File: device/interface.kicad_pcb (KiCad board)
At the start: 2 copper layers, 43.2 x 64.1 mm, 30 parts, among them IC1 ATTINY2313-S, J1 Screw_Terminal_1x02, J2 Screw_Terminal_01x02, P1 CONN_01X06, P2 CONN_02X03, P3 CONN_01X04, U1 L7805, U2 MAX483E, Y1 16MHz

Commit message: pcb update
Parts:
- moved J1 0.63 mm to (99.1, 61.6)
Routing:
- net +5V: track 127.5 -> 128.4 mm
- net /MOSI: track 28.8 -> 29.6 mm
- net /SCK: track 24.3 -> 25.0 mm
- net GND: track 157.1 -> 156.4 mm
- net +24V: track 43.4 -> 44.0 mm
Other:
- outline, holes or cut-outs redrawn
- net class RS-485 added: clearance 0.5, trace_width 0.5, via_dia 0.8, via_drill 0.4

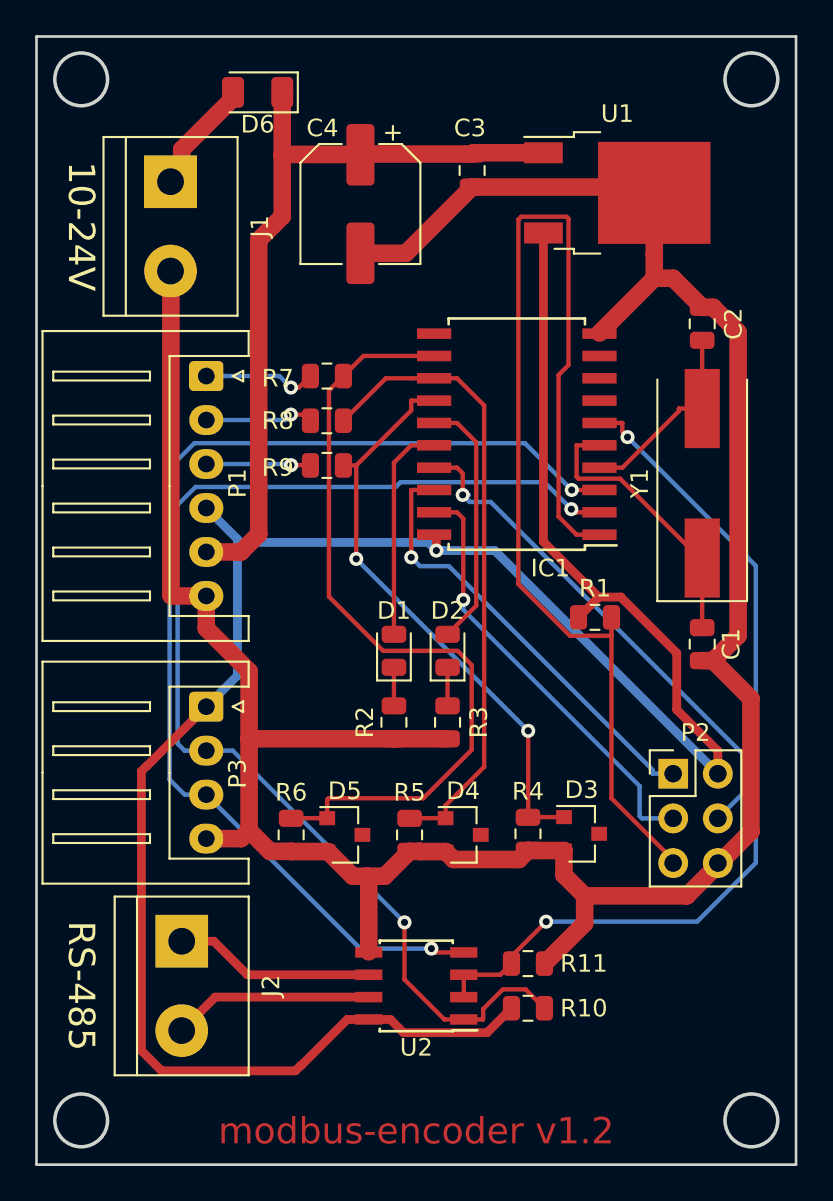
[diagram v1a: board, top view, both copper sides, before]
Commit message: added address switch
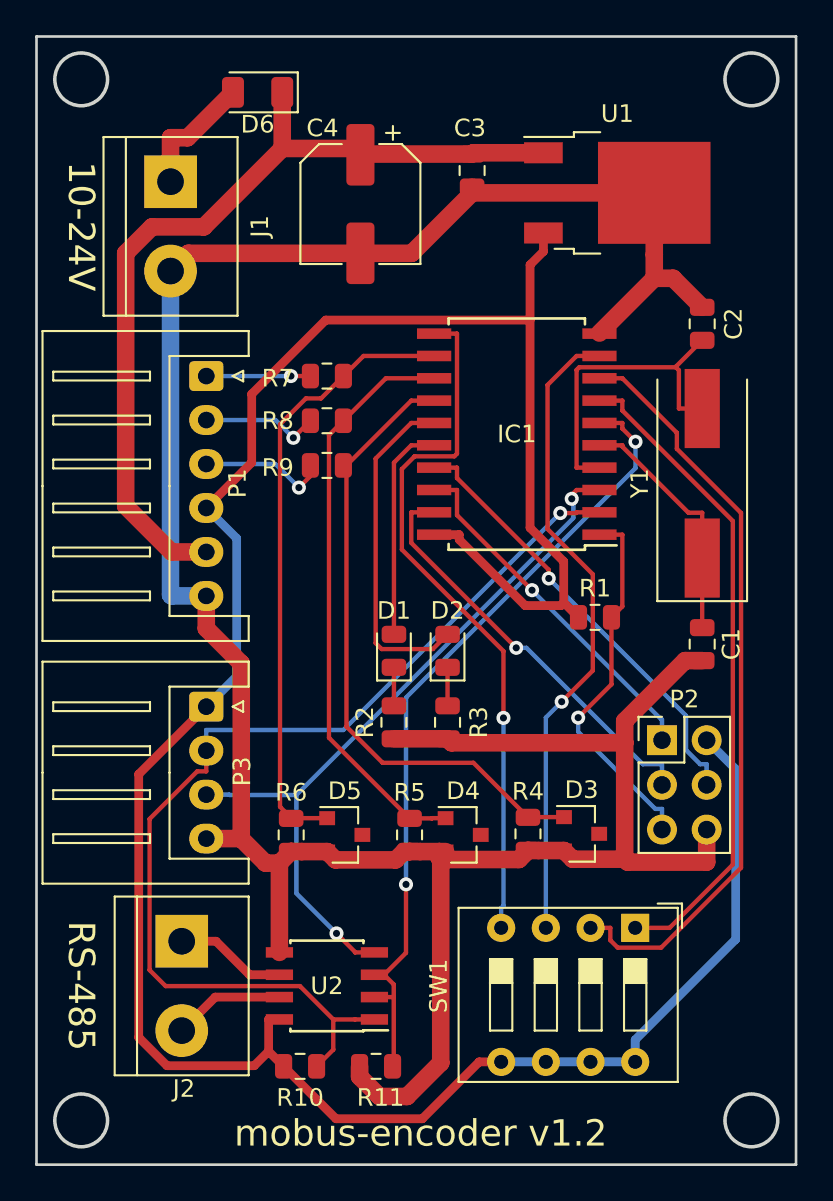
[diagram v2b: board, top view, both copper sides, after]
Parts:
- added SW1: SW_DIP_x04, Button_Switch_THT:SW_DIP_SPSTx04_Slide_9.78x12.34mm_W7.62mm_P2.54mm, F.Cu at (125.5, 104.0)
- moved R10 13.4 mm to (106.4, 111.9)
- moved R11 10.4 mm to (110.7, 111.9), turned to 180 degrees
- moved U2 5.08 mm to (108.0, 107.3)
- moved P2 2.01 mm to (127.0, 93.3)
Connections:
- IC1 pad 11: Net-(IC1-Pad11) -> /A3
- IC1 pad 7: Net-(IC1-Pad7) -> /A0
- IC1 pad 8: Net-(IC1-Pad8) -> /A1
- IC1 pad 9: Net-(IC1-Pad9) -> /A2
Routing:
- net /RST: track 65.4 -> 21.3 mm, vias 0 -> 1
- net /A1: track 0.00 -> 43.2 mm
- net /A3: track 0.00 -> 40.2 mm, vias 0 -> 1
- net /A0: track 0.00 -> 37.3 mm
- net /A2: track 0.00 -> 36.7 mm, vias 0 -> 1
- net /TX: track 64.6 -> 41.9 mm
- net +5V: track 128.4 -> 146.7 mm, vias 1 -> 0
- net /PHASEA: track 45.6 -> 35.1 mm
- net /RX: track 69.5 -> 59.8 mm, vias 2 -> 1
- net Net-(C2-Pad1): track 11.5 -> 18.5 mm
- net +24V: track 44.0 -> 49.6 mm
- net Net-(J2-Pad1): track 11.4 -> 6.34 mm
- net Net-(J2-Pad2): track 11.4 -> 6.34 mm
- net /RDE: track 51.0 -> 46.0 mm
- net /MISO: track 25.2 -> 20.4 mm
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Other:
- board text added: "mobus-encoder v1.2"
- board text removed: "modbus-encoder v1.2"

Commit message: render
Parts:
- added REF**: KiCad-Logo2_6mm_SilkScreen, Symbol:KiCad-Logo2_6mm_SilkScreen, B.Cu at (113.3, 58.8)
- SW1: value SW_DIP_x04 -> ADDRESS_SW
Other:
- board text added: "modbus-encoder v1.2"
- board text removed: "mobus-encoder v1.2"
